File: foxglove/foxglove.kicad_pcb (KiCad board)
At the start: 4 copper layers, 77.4 x 53.3 mm, 108 parts, among them IC1 LFE5U-12F-6BG256C, J1 NEIGHBOR1, J2 NEIGHBOR2, J3 Conn_02x05_Odd_Even, J4 Conn_02x05_Odd_Even, J5 Conn_01x02_Female, J6 Conn_02x03_Odd_Even, J7 BONUS_ROW, U10 SHIFTER, U11 74HC4051, U12 SHIFTER, U13 74HC4051, U14 SHIFTER, U15 74HC4051, U16 SHIFTER, U17 74HC4051, U18 SHIFTER, U19 74HC4051, U2 ADP225, U20 SHIFTER, U21 74HC4051, U22 SHIFTER, U23 74HC4051, U24 SHIFTER, U25 74LVC1G53, U3 MC4558CPT, U4 74LVC1G3157, U5 LM339, U6 ADP225, U7 DAC084S085, U8 74AHC1G04, U9 74HC4051

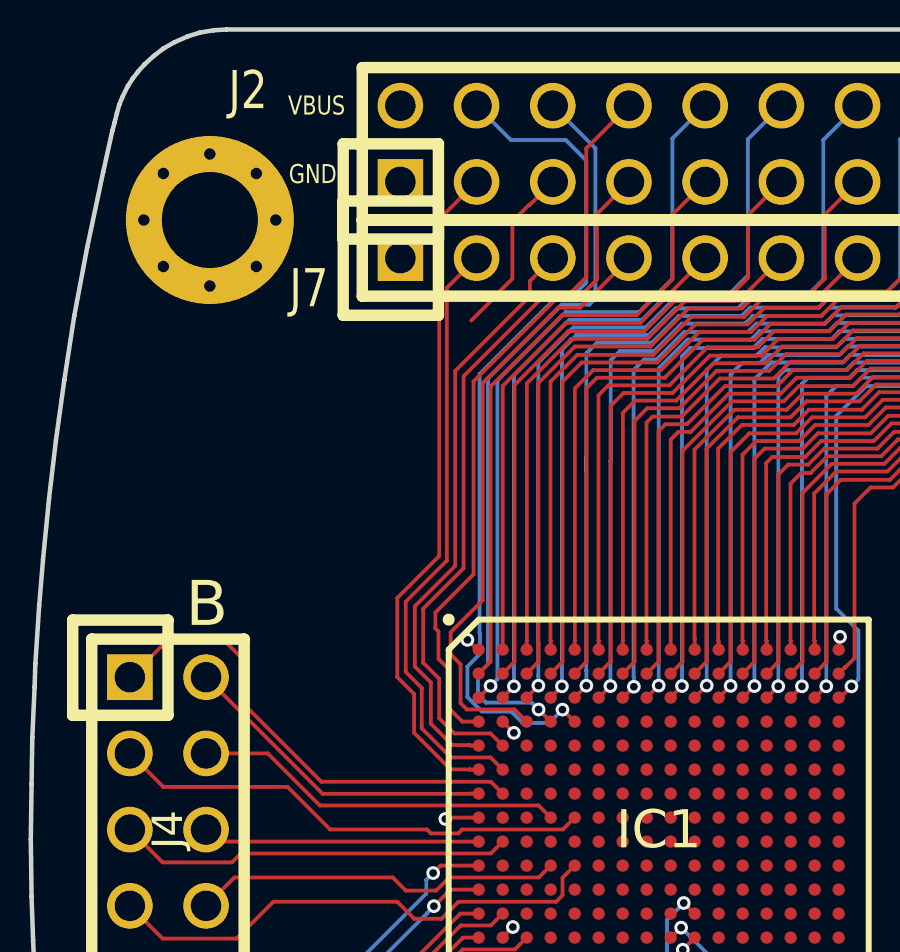
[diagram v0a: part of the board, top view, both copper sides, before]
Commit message: Connected bank B to VCCIO7 pins, switched out voltage regulators
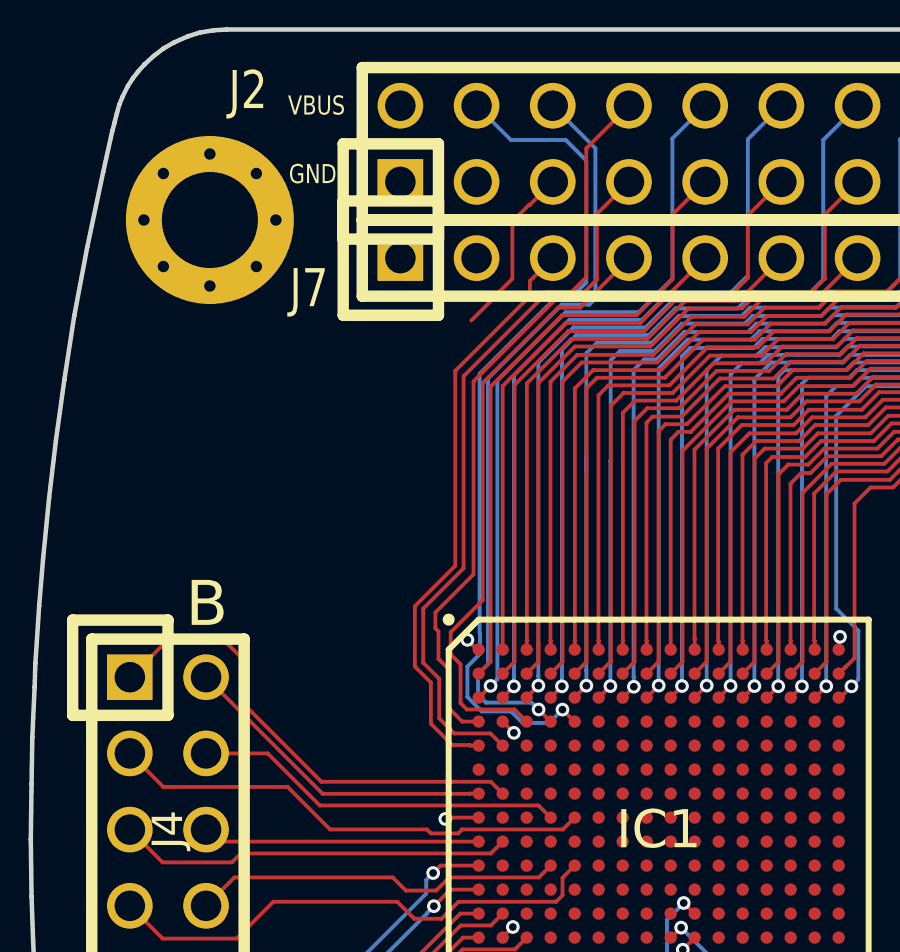
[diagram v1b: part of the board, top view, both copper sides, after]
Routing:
- net /J2.03: track 22.4 -> 0.00 mm
- net /J7.02: track 20.1 -> 0.00 mm
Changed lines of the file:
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@@
     (thickness 1.6)
     (drawings 123)
-    (tracks 1959)
+    (tracks 1940)
     (zones 0)
     (modules 108)
@@
   (gr_line (start 176.53 121.92) (end 116.1288 121.92) (angle 90) (layer Edge.Cuts) (width 0.15))
   (gr_line (start 116.1288 68.58) (end 176.53 68.58) (angle 90) (layer Edge.Cuts) (width 0.15))
-  (segment (start 129.54 76.2) (end 129.54 76.2254) (width 0.127) (layer F.Cu) (net 161))
-  (segment (start 129.54 76.2254) (end 127.9144 77.851) (width 0.127) (layer F.Cu) (net 161))
   (via (at 123.4186 94.8944) (size 0.4572) (drill 0.254) (layers F.Cu B.Cu) (net 1))
   (segment (start 124.5306 94.85) (end 123.463 94.85) (width 0.127) (layer F.Cu) (net 1))
@@
   (segment (start 128.1176 72.9488) (end 127.4318 72.263) (width 0.127) (layer B.Cu) (net 159))
   (segment (start 127.4318 72.263) (end 125.603 72.263) (width 0.127) (layer B.Cu) (net 159))
-  (segment (start 124.240687 93.25) (end 124.234087 93.2434) (width 0.127) (layer F.Cu) (net 160))
-  (segment (start 124.5306 93.25) (end 124.240687 93.25) (width 0.127) (layer F.Cu) (net 160))
-  (segment (start 124.234087 93.2434) (end 123.5964 93.2434) (width 0.127) (layer F.Cu) (net 160))
-  (segment (start 123.5964 93.2434) (end 122.3772 92.0242) (width 0.127) (layer F.Cu) (net 160))
-  (segment (start 122.3772 92.0242) (end 122.3772 90.7288) (width 0.127) (layer F.Cu) (net 160))
-  (segment (start 122.3772 90.7288) (end 121.8184 90.17) (width 0.127) (layer F.Cu) (net 160))
-  (segment (start 121.8184 90.17) (end 121.8184 87.5284) (width 0.127) (layer F.Cu) (net 160))
-  (segment (start 121.8184 87.5284) (end 123.2154 86.1314) (width 0.127) (layer F.Cu) (net 160))
-  (segment (start 123.2154 74.9046) (end 124.46 73.66) (width 0.127) (layer F.Cu) (net 160))
-  (segment (start 123.2154 86.1314) (end 123.2154 74.9046) (width 0.127) (layer F.Cu) (net 160))
+  (segment (start 129.54 76.2) (end 129.54 76.2254) (width 0.127) (layer F.Cu) (net 161))
+  (segment (start 129.54 76.2254) (end 127.9144 77.851) (width 0.127) (layer F.Cu) (net 161))
   (segment (start 124.138501 91.245501) (end 125.726101 91.245501) (width 0.127) (layer F.Cu) (net 161))
   (segment (start 123.9266 89.7382) (end 123.9266 91.0336) (width 0.127) (layer F.Cu) (net 161))
@@
   (segment (start 126.238001 77.469999) (end 123.7488 79.9592) (width 0.127) (layer F.Cu) (net 162))
   (segment (start 123.7488 79.9592) (end 123.7488 86.457976) (width 0.127) (layer F.Cu) (net 162))
-  (segment (start 124.926101 92.845501) (end 123.604901 92.845501) (width 0.127) (layer F.Cu) (net 163))
-  (segment (start 125.3306 93.25) (end 124.926101 92.845501) (width 0.127) (layer F.Cu) (net 163))
-  (segment (start 123.604901 92.845501) (end 122.6312 91.8718) (width 0.127) (layer F.Cu) (net 163))
-  (segment (start 122.6312 91.8718) (end 122.6312 90.5256) (width 0.127) (layer F.Cu) (net 163))
-  (segment (start 122.6312 90.5256) (end 122.0978 89.9922) (width 0.127) (layer F.Cu) (net 163))
-  (segment (start 122.0978 89.9922) (end 122.0978 87.6554) (width 0.127) (layer F.Cu) (net 163))
-  (segment (start 122.0978 87.6554) (end 123.4694 86.2838) (width 0.127) (layer F.Cu) (net 163))
-  (segment (start 123.4694 77.1906) (end 124.46 76.2) (width 0.127) (layer F.Cu) (net 163))
-  (segment (start 123.4694 86.2838) (end 123.4694 77.1906) (width 0.127) (layer F.Cu) (net 163))
   (via (at 130.539478 100.033527) (size 0.4572) (drill 0.254) (layers F.Cu B.Cu) (net 164))
   (segment (start 130.9306 99.65) (end 130.923005 99.65) (width 0.127) (layer F.Cu) (net 164))

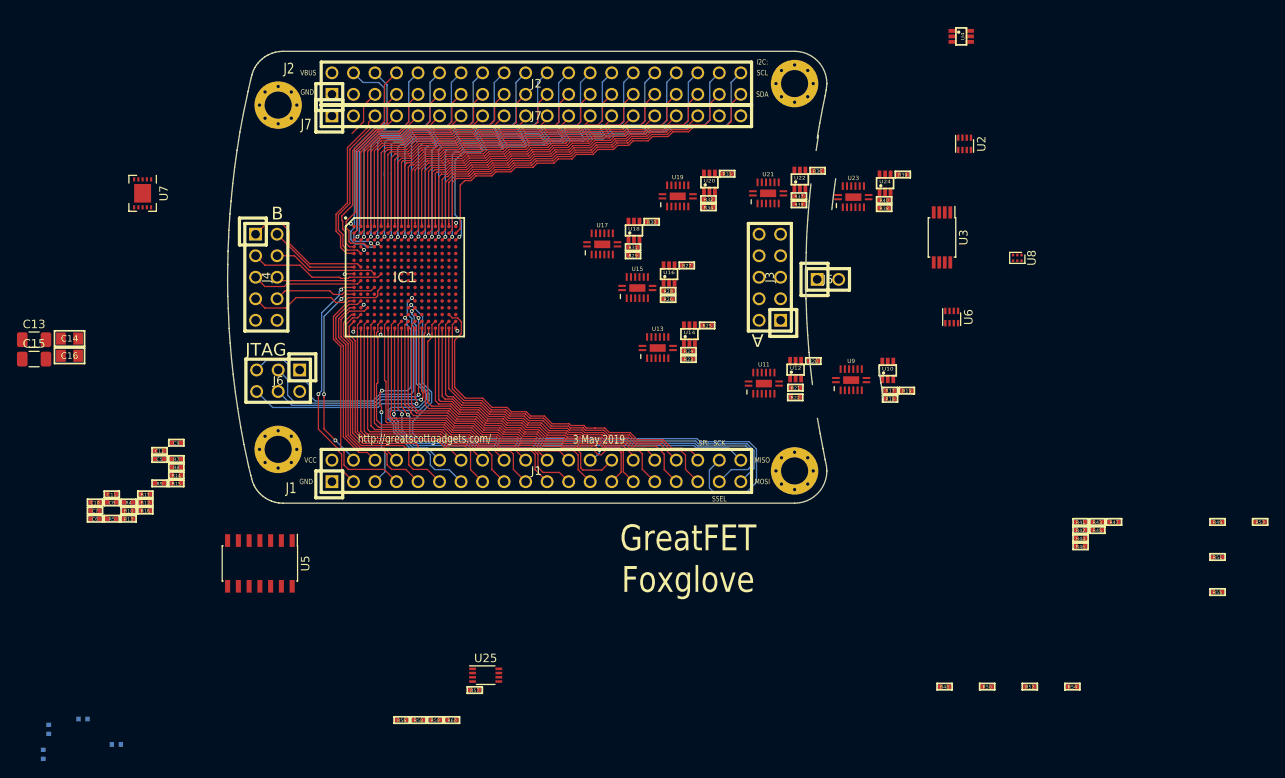
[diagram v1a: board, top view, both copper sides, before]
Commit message: Routed bank B to FPGA VCCIO7, added bypass caps
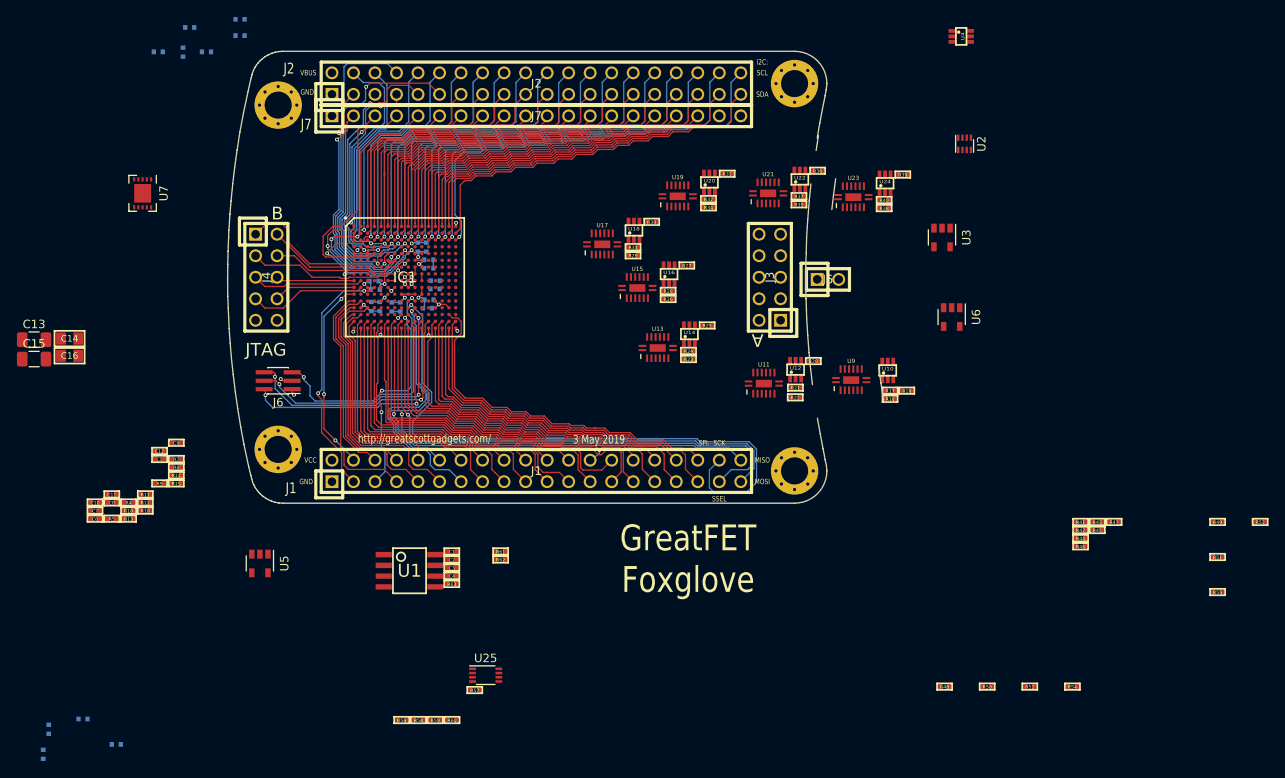
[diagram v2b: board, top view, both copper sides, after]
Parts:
- removed U8: 74AHC1G04, Package_TO_SOT_SMD:SOT-886
- added C1: 1uF, gsg-modules:0402, F.Cu at (136.1, 127.6)
- added C17: 100nF, gsg-modules:0402, B.Cu at (101.4, 68.6)
- added C18: 100nF, gsg-modules:0402, B.Cu at (134.1, 95.7)
- added C19: 100nF, gsg-modules:0402, B.Cu at (107.1, 68.6)
- added C2: 4.7uF, gsg-modules:0402, F.Cu at (136.1, 128.6)
- added C20: 10nF, gsg-modules:0402, B.Cu at (104.3, 68.7)
- added C21: 10nF, gsg-modules:0402, B.Cu at (134.1, 96.6)
- added C22: 10nF, gsg-modules:0402, B.Cu at (105.1, 65.8)
- added C23: 100nF, gsg-modules:0402, B.Cu at (133.0, 91.7)
- added C24: 100nF, gsg-modules:0402, B.Cu at (133.2, 98.9)
- added C25: 100nF, gsg-modules:0402, B.Cu at (126.6, 98.7)
- added C26: 10nF, gsg-modules:0402, B.Cu at (132.1, 91.7)
- added C27: 10nF, gsg-modules:0402, B.Cu at (133.4, 97.9)
- added C28: 10nF, gsg-modules:0402, B.Cu at (127.6, 98.7)
- added C29: 100nF, gsg-modules:0402, B.Cu at (127.0, 96.7)
- added C3: 2.7nF, gsg-modules:0402, F.Cu at (136.1, 129.5)
- added C30: 100nF, gsg-modules:0402, B.Cu at (133.3, 94.2)
- added C31: 10nF, gsg-modules:0402, B.Cu at (126.9, 95.7)
- added C32: 10nF, gsg-modules:0402, B.Cu at (133.3, 93.2)
- added C33: 100nF, gsg-modules:0402, B.Cu at (129.0, 98.8)
- added C34: 100nF, gsg-modules:0402, B.Cu at (111.1, 66.7)
- added C35: 10nF, gsg-modules:0402, B.Cu at (130.0, 98.8)
- added C36: 10nF, gsg-modules:0402, B.Cu at (111.1, 64.8)
- added C4: 1uF, gsg-modules:0402, F.Cu at (136.1, 130.5)
- added R61: 10k, gsg-modules:0402, F.Cu at (141.8, 127.6)
- added R62: 10k, gsg-modules:0402, F.Cu at (141.8, 128.6)
- added R63: 127.2k, gsg-modules:0402, F.Cu at (136.1, 131.4)
- added U1: LM393, gsg-modules:SOIC8-154, F.Cu at (131.1, 129.9)
- C10: value 1uF -> 4.7uF
- C11, C12: value 1uF -> 2.7nF
- C8: value 0.1uF -> 1uF
- C9: value 0.1uF -> 4.7uF
- J6: footprint gsg-modules:HEADER-2x3 -> Connector_PinHeader_1.00mm:PinHeader_2x03_P1.00mm_Vertical_SMD
- R11: value 165k -> 20k
- R12: value 20k -> 57.25k
- R13: value 217k -> 20k
- R14: value 165k -> 118.1k
- R16: value 20k -> 118.1k
- R18, R19, R24, R25, R27, R28, R30, R31, R33, R34, R36, R37, R39, R40, R46, R47: value R -> 10k
- R21: value R -> 20k
- R22: value R -> 89.8k
- R8: value 217k -> 89.8k
- U3: value MC4558CPT -> AP2127; footprint Package_SO:TSSOP-8_4.4x3mm_P0.65mm -> Package_TO_SOT_SMD:SOT-23-5
- U5: value LM339 -> AP2127; footprint Package_SO:SOIC-14_3.9x8.7mm_P1.27mm -> Package_TO_SOT_SMD:SOT-23-5
- U6: value ADP225 -> AP2127; footprint Package_CSP:LFCSP-8_2x2mm_P0.5mm -> Package_TO_SOT_SMD:SOT-23-5
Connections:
- net /sheet5CF421BE/A_FPGA renamed Net-(R48-Pad1)
- net /sheet5D17D613/A_FPGA renamed Net-(R49-Pad1)
- net /sheet5D190CFC/A_FPGA renamed Net-(R50-Pad1)
- net /sheet5D190CFD/A_FPGA renamed Net-(R51-Pad1)
- net /sheet5D1A4642/A_FPGA renamed Net-(R52-Pad1)
- net /sheet5D1A4643/A_FPGA renamed Net-(R53-Pad1)
- net /sheet5D1A4644/A_FPGA renamed Net-(R54-Pad1)
- net /sheet5D1A4645/A_FPGA renamed Net-(R55-Pad1)
- C10 pad 1: /A1 -> GND
- C10 pad 2: GND -> /VCCB
- C11 pad 1: +5V -> /DAC
- C11 pad 2: GND -> Net-(C11-Pad2)
- C12 pad 1: /VCCA -> /VCCB
- C12 pad 2: GND -> Net-(C12-Pad2)
- C8 pad 1: +5V -> GND
- C8 pad 2: GND -> VCC
- C9 pad 2: +5V -> /DAC
- IC1 pad B1: /J2.09 -> (no net)
- IC1 pad B2: /J2.11 -> (no net)
- IC1 pad C1: /J2.10 -> (no net)
- IC1 pad C2: /J2.12 -> (no net)
- IC1 pad C3: /J2.14 -> (no net)
- IC1 pad D1: /J2.07 -> (no net)
- IC1 pad D3: /J7.04 -> (no net)
- IC1 pad D4: /J2.06 -> /J2.07
- IC1 pad D5: /J2.04 -> /J7.04
- IC1 pad D6: (no net) -> /J2.06
- IC1 pad D7: (no net) -> /J2.04
- IC1 pad D8: (no net) -> /J2.09
- IC1 pad D9: (no net) -> /J2.11
- IC1 pad E1: /J7.03 -> (no net)
- IC1 pad E10: (no net) -> /J2.14
- IC1 pad E2: /J2.08 -> (no net)
- IC1 pad E4: (no net) -> /J7.03
- IC1 pad E5: (no net) -> /J2.08
- IC1 pad E6: (no net) -> /J2.03
- IC1 pad E7: (no net) -> /J7.02
- IC1 pad E8: (no net) -> /J2.10
- IC1 pad E9: (no net) -> /J2.12
- IC1 pad F1: /J2.03 -> (no net)
- IC1 pad F10: (no net) -> VCC
- IC1 pad F11: (no net) -> VCC
- IC1 pad F2: /J7.02 -> (no net)
- IC1 pad F6: (no net) -> VCC
- IC1 pad F7: (no net) -> VCC
- IC1 pad H11: (no net) -> VCC
- IC1 pad H6: (no net) -> /VCCB
- IC1 pad H7: (no net) -> /VCCB
- IC1 pad J11: (no net) -> VCC
- IC1 pad J6: (no net) -> VCC
- IC1 pad J7: (no net) -> VCC
- IC1 pad K1: /J1.03 -> /B8
- IC1 pad K11: (no net) -> VCC
- IC1 pad K2: (no net) -> /B7
- IC1 pad K4: /B8 -> /J1.03
- IC1 pad K5: /B7 -> (no net)
- IC1 pad L11: (no net) -> VCC
- J3 pad 2: /A1 -> /A2
- J3 pad 3: /A1 -> /A3
- J3 pad 4: /A1 -> /A4
- J3 pad 5: /A1 -> /A5
- J3 pad 6: /A1 -> /A6
- J3 pad 7: /A1 -> /A7
- J3 pad 8: /A1 -> /A8
- J4 pad 9: VCC -> /VCCB
- J6 pad 2: GND -> /TCK
- J6 pad 3: /TDI -> GND
- J6 pad 4: /TMS -> /TDI
- J6 pad 6: /TCK -> /TMS
- R11 pad 1: /A1 -> GND
- R11 pad 2: Net-(R11-Pad2) -> Net-(C11-Pad2)
- R12 pad 1: GND -> /VCCB
- R12 pad 2: Net-(R11-Pad2) -> Net-(C12-Pad2)
- R13 pad 1: Net-(R13-Pad1) -> GND
- R13 pad 2: Net-(R13-Pad2) -> Net-(C12-Pad2)
- R14 pad 1: /VCCA -> /DAC1
- R14 pad 2: Net-(R13-Pad2) -> Net-(C3-Pad2)
- R15 pad 2: Net-(R15-Pad2) -> /SSEL
- R16 pad 1: Net-(R13-Pad2) -> /DAC2
- R16 pad 2: GND -> Net-(C11-Pad2)
- R21 pad 1: Net-(R21-Pad1) -> GND
- R21 pad 2: GND -> Net-(C3-Pad2)
- R22 pad 1: Net-(R22-Pad1) -> /VCCA
- R22 pad 2: /VCCA -> Net-(C3-Pad2)
- R24 pad 1: Net-(R24-Pad1) -> GND
- R24 pad 2: GND -> Net-(R24-Pad2)
- R25 pad 1: Net-(R25-Pad1) -> /VCCA
- R25 pad 2: /VCCA -> Net-(R25-Pad2)
- R27 pad 1: Net-(R27-Pad1) -> GND
- R27 pad 2: GND -> Net-(R27-Pad2)
- R28 pad 1: Net-(R28-Pad1) -> /VCCA
- R28 pad 2: /VCCA -> Net-(R28-Pad2)
- R30 pad 1: Net-(R30-Pad1) -> GND
- R30 pad 2: GND -> Net-(R30-Pad2)
- R31 pad 1: Net-(R31-Pad1) -> /VCCA
- R31 pad 2: /VCCA -> Net-(R31-Pad2)
- R33 pad 1: Net-(R33-Pad1) -> GND
- R33 pad 2: GND -> Net-(R33-Pad2)
- R34 pad 1: Net-(R34-Pad1) -> /VCCA
- R34 pad 2: /VCCA -> Net-(R34-Pad2)
- R36 pad 1: Net-(R36-Pad1) -> GND
- R36 pad 2: GND -> Net-(R36-Pad2)
- R37 pad 1: Net-(R37-Pad1) -> /VCCA
- R37 pad 2: /VCCA -> Net-(R37-Pad2)
- R39 pad 1: Net-(R39-Pad1) -> GND
- R39 pad 2: GND -> Net-(R39-Pad2)
- R40 pad 1: Net-(R40-Pad1) -> /VCCA
- R40 pad 2: /VCCA -> Net-(R40-Pad2)
- R47 pad 1: Net-(R47-Pad1) -> /VCCA
- R47 pad 2: /VCCA -> Net-(R47-Pad2)
- R49 pad 2: /A1 -> /A2
- R50 pad 2: /A1 -> /A3
- R51 pad 2: /A1 -> /A4
- R52 pad 2: /A1 -> /A5
- R53 pad 2: /A1 -> /A6
- R54 pad 2: /A1 -> /A7
- R55 pad 2: /A1 -> /A8
- R8 pad 1: Net-(R11-Pad2) -> /DAC
- R8 pad 2: Net-(R8-Pad2) -> Net-(C11-Pad2)
- U11 pad 1: /ADC_A -> /COMP1
- U11 pad 12: /VCCA -> /DAC
- U11 pad 13: Net-(R21-Pad1) -> Net-(R27-Pad2)
- U11 pad 14: Net-(R22-Pad1) -> Net-(R28-Pad2)
- U11 pad 15: GND -> /ADC_A
- U11 pad 2: /DAC3 -> (no net)
- U11 pad 4: /COMP1 -> (no net)
- U11 pad 5: /A1 -> /COMP2
- U13 pad 1: /ADC_A -> /COMP1
- U13 pad 12: /VCCA -> /DAC
- U13 pad 13: Net-(R24-Pad1) -> Net-(R30-Pad2)
- U13 pad 14: Net-(R25-Pad1) -> Net-(R31-Pad2)
- U13 pad 15: GND -> /ADC_A
- U13 pad 2: /DAC3 -> (no net)
- U13 pad 4: /COMP1 -> (no net)
- U13 pad 5: /A1 -> /COMP2
- U15 pad 1: /ADC_A -> /COMP1
- U15 pad 12: /VCCA -> /DAC
- U15 pad 13: Net-(R27-Pad1) -> Net-(R33-Pad2)
- U15 pad 14: Net-(R28-Pad1) -> Net-(R34-Pad2)
- U15 pad 15: GND -> /ADC_A
- U15 pad 2: /DAC3 -> (no net)
- U15 pad 4: /COMP1 -> (no net)
- U15 pad 5: /A1 -> /COMP2
- U17 pad 1: /ADC_A -> /COMP1
- U17 pad 12: /VCCA -> /DAC
- U17 pad 13: Net-(R30-Pad1) -> Net-(R36-Pad2)
- U17 pad 14: Net-(R31-Pad1) -> Net-(R37-Pad2)
- U17 pad 15: GND -> /ADC_A
- U17 pad 2: /DAC3 -> (no net)
- U17 pad 4: /COMP1 -> (no net)
- U17 pad 5: /A1 -> /COMP2
- U19 pad 1: /ADC_A -> /COMP1
- U19 pad 12: /VCCA -> /DAC
- U19 pad 13: Net-(R33-Pad1) -> Net-(R39-Pad2)
- U19 pad 14: Net-(R34-Pad1) -> Net-(R40-Pad2)
- U19 pad 15: GND -> /ADC_A
- U19 pad 2: /DAC3 -> (no net)
- U19 pad 4: /COMP1 -> (no net)
- U19 pad 5: /A1 -> /COMP2
- U21 pad 1: /ADC_A -> /COMP1
- U21 pad 12: /VCCA -> /DAC
- U21 pad 13: Net-(R36-Pad1) -> Net-(R46-Pad2)
- U21 pad 14: Net-(R37-Pad1) -> Net-(R47-Pad2)
- U21 pad 15: GND -> /ADC_A
- U21 pad 2: /DAC3 -> (no net)
- U21 pad 4: /COMP1 -> (no net)
- U21 pad 5: /A1 -> /COMP2
- U23 pad 1: /ADC_A -> /COMP1
- U23 pad 12: /VCCA -> /DAC
- U23 pad 13: Net-(R39-Pad1) -> Net-(R61-Pad2)
- U23 pad 14: Net-(R40-Pad1) -> Net-(R62-Pad2)
- U23 pad 15: GND -> /ADC_A
- U23 pad 2: /DAC3 -> (no net)
- U23 pad 4: /COMP1 -> (no net)
- U23 pad 5: /A1 -> /COMP2
- U25 pad 6: Net-(R47-Pad1) -> Net-(R19-Pad1)
- U25 pad 7: Net-(R46-Pad2) -> Net-(R18-Pad1)
- U3 pad 1: /DAC3 -> +5V
- U3 pad 2: /DAC3 -> GND
- U3 pad 3: Net-(U3-Pad3) -> (no net)
- U3 pad 4: GND -> Net-(C3-Pad2)
- U3 pad 5: Net-(U3-Pad5) -> /VCCA
- U5 pad 1: (no net) -> +5V
- U5 pad 2: (no net) -> GND
- U5 pad 3: +5V -> (no net)
- U5 pad 4: /A1 -> Net-(C11-Pad2)
- U5 pad 5: /COMP1 -> /DAC
- U6 pad 1: (no net) -> VCC
- U6 pad 2: (no net) -> GND
- U6 pad 3: GND -> (no net)
- U6 pad 4: Net-(R11-Pad2) -> Net-(C12-Pad2)
- U6 pad 5: /A1 -> /VCCB
- U7 pad 2: Net-(R13-Pad1) -> /DAC1
- U7 pad 3: Net-(R8-Pad2) -> /DAC2
- U7 pad 4: Net-(U3-Pad3) -> /DAC3
- U7 pad 5: Net-(U3-Pad5) -> /DAC4
- U7 pad 9: Net-(R15-Pad2) -> /SSEL
- U9 pad 1: /ADC_A -> /COMP1
- U9 pad 12: /VCCA -> /DAC
- U9 pad 13: Net-(R18-Pad1) -> Net-(R24-Pad2)
- U9 pad 14: Net-(R19-Pad1) -> Net-(R25-Pad2)
- U9 pad 15: GND -> /ADC_A
- U9 pad 2: /DAC3 -> (no net)
- U9 pad 4: /COMP1 -> (no net)
- U9 pad 5: /A1 -> /COMP2
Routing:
- net /J2.03: track 0.00 -> 27.4 mm, vias 0 -> 2
- net GND: track 5.65 -> 32.5 mm, vias 9 -> 20
- net /J7.02: track 0.00 -> 26.3 mm, vias 0 -> 2
- net /J2.14: track 28.2 -> 47.3 mm, vias 1 -> 3
- net /J2.12: track 26.2 -> 43.4 mm, vias 1 -> 3
- net /J2.11: track 22.7 -> 39.8 mm, vias 0 -> 2
- net /J2.10: track 24.3 -> 38.5 mm, vias 1 -> 3
- net VCC: track 0.00 -> 13.3 mm, vias 0 -> 5
- net /J2.09: track 21.0 -> 34.1 mm, vias 0 -> 2
- net +1V1: track 0.00 -> 8.87 mm, vias 0 -> 2
- net /J2.08: track 26.4 -> 35.3 mm, vias 0 -> 1
- net /J7.03: track 19.5 -> 26.0 mm
- net /TDO: track 35.0 -> 29.1 mm, vias 1 -> 2
- net /ADC: track 5.76 -> 0.00 mm
- net /J7.04: track 20.3 -> 24.3 mm, vias 0 -> 2
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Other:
- rule solder_mask_min_width: 0.25 -> 0.001

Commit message: Routed ADC/DAC and FPGA passives
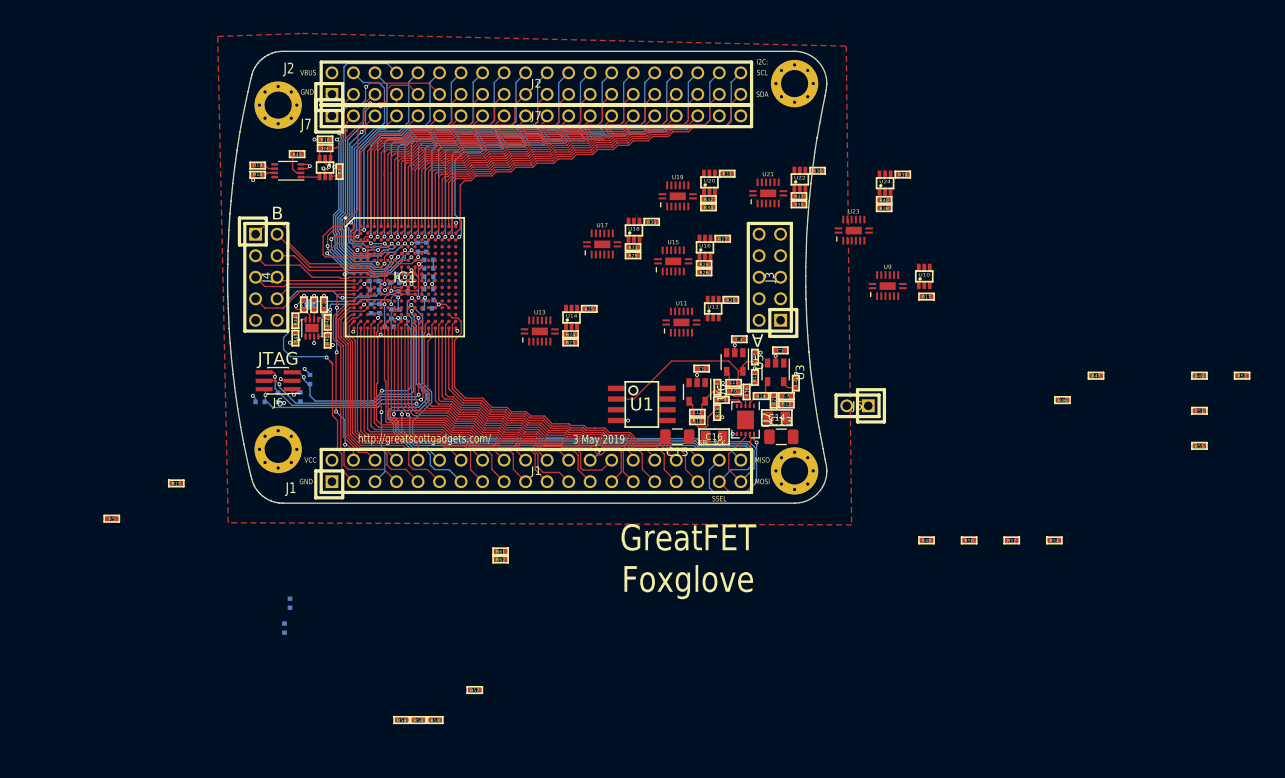
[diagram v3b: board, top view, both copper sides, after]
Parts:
- removed C17: 100nF, gsg-modules:0402
- removed C20: 10nF, gsg-modules:0402
- added TP1: TestPoint, gsg-modules:TESTPOINT-50MIL, B.Cu at (121.3, 99.6)
- added TP2: TestPoint, gsg-modules:TESTPOINT-50MIL, B.Cu at (119.3, 98.5)
- R4, R60: moved to B.Cu
- U2: footprint Package_CSP:LFCSP-8_2x2mm_P0.5mm -> gsg-modules:SON50P200X200X60-9N
- moved R45 104.4 mm to (117.8, 80.7)
- moved R43 97.1 mm to (117.6, 102.4), turned to 90 degrees
- moved R44 96.2 mm to (117.6, 100.4), turned to 90 degrees
- moved R42 92.2 mm to (121.4, 100.6), turned to 270 degrees
- moved R41 91.4 mm to (121.4, 102.7), turned to 270 degrees
- moved C13 88.9 mm to (175.0, 114.1)
- moved C14 84.0 mm to (174.4, 111.8), turned to 180 degrees
- moved R19 81.1 mm to (113.2, 82.1), turned to 180 degrees
- moved U2 80.0 mm to (119.6, 101.2), turned to 90 degrees
- moved R18 79.2 mm to (113.2, 83.2), turned to 180 degrees
- moved C16 76.7 mm to (167.0, 114.1)
- moved U4 76.7 mm to (121.1, 82.3), turned to 180 degrees
- moved C15 76.5 mm to (162.7, 114.1), turned to 180 degrees
- moved U7 76.0 mm to (170.7, 112.1)
- moved C10 74.7 mm to (167.4, 108.2), turned to 270 degrees
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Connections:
- IC1 pad F6: VCC -> /VCCIO0
- IC1 pad F7: VCC -> /VCCIO0
- IC1 pad R7: /J1.24 -> (no net)
- J1 pad 24: /J1.24 -> /CSSPIN
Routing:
- net /CSSPIN: track 0.00 -> 36.9 mm
- net /J1.24: track 34.6 -> 0.00 mm
- net +1V1: track 8.87 -> 32.6 mm, vias 2 -> 5
- net GND: track 32.5 -> 54.9 mm, vias 20 -> 43
- net /DAC: track 0.00 -> 22.0 mm
- net +2V5: track 2.21 -> 22.2 mm, vias 1 -> 3
- net VCC: track 13.3 -> 27.1 mm, vias 5 -> 10
- net /ADC: track 0.00 -> 11.4 mm
- net /SSEL: track 61.8 -> 72.5 mm
- net /J1.03: track 29.3 -> 39.9 mm
- net Net-(C12-Pad2): track 0.00 -> 8.16 mm
- net /MOSI: track 58.7 -> 65.7 mm
- net /VCCB: track 0.80 -> 7.64 mm, vias 0 -> 1
- net Net-(C11-Pad2): track 0.00 -> 6.82 mm
- net Net-(C3-Pad2): track 0.00 -> 4.74 mm
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- added copper zone on F.Cu, net +5V
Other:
- board size 77.4 x 53.3 mm -> 70.7 x 53.3 mm
